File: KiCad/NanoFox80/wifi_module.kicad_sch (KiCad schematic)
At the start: 8 parts, among them U201 TPS22810DBVT, U202 74HC1G08

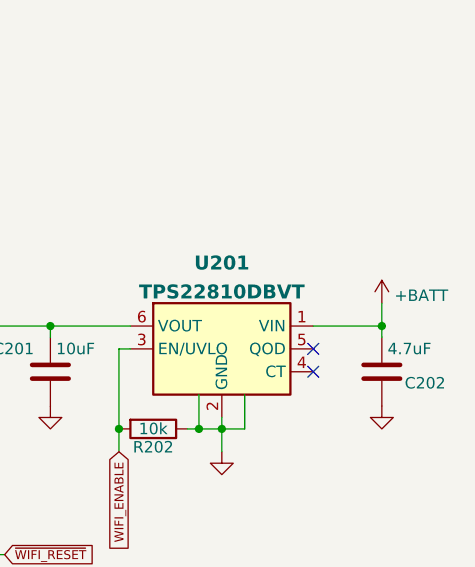
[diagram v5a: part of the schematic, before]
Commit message: +BATT Fix
Schematic change
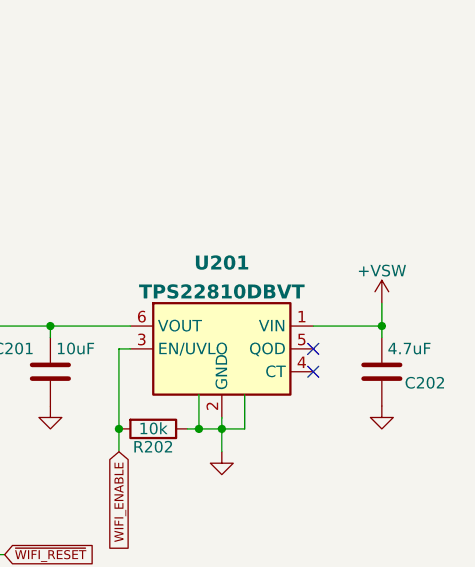
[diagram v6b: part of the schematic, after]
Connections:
- net +BATT renamed +VSW
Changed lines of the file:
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@@
     (pin "1")
   )
-  (symbol (lib_id "power:+BATT") (at 246.38 83.82 0) (unit 1)
+  (symbol (lib_id "power:+VSW") (at 246.38 83.82 0) (unit 1)
     (in_bom yes) (on_board yes) (fields_autoplaced)
-    (property "Reference" "#PWR0203" (id 0) (at 246.38 87.63 0)
+    (property "Reference" "#PWR?" (id 0) (at 246.38 87.63 0)
       (effects (font (size 1.27 1.27)) hide)
     )
-    (property "Value" "+BATT" (id 1) (at 247.777 82.9838 0)
-      (effects (font (size 1.27 1.27)) (justify left))
-    )
+    (property "Value" "+VSW" (id 1) (at 246.38 80.2442 0))
     (property "Footprint" "" (id 2) (at 246.38 83.82 0)
       (effects (font (size 1.27 1.27)) hide)
